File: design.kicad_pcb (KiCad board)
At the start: 2 copper layers, 28.5 x 12 mm, 7 parts, among them J1 USB_C_Receptacle, J2 Conn_01x05, U1 ATtiny1616-M

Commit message: PCB add ID
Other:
- board text added: "<<ID>>"
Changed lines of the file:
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@@
   (general
     (thickness 1.6)
-    (drawings 8)
+    (drawings 9)
     (tracks 0)
     (zones 0)
@@
     )
   )
+  (gr_text <<ID>> (at 151.3 81.8 180) (layer B.SilkS)
+    (effects (font (size 1 1) (thickness 0.15)) (justify mirror))
+  )
   (gr_text <<date>> (at 151.3 86.4 180) (layer B.SilkS)

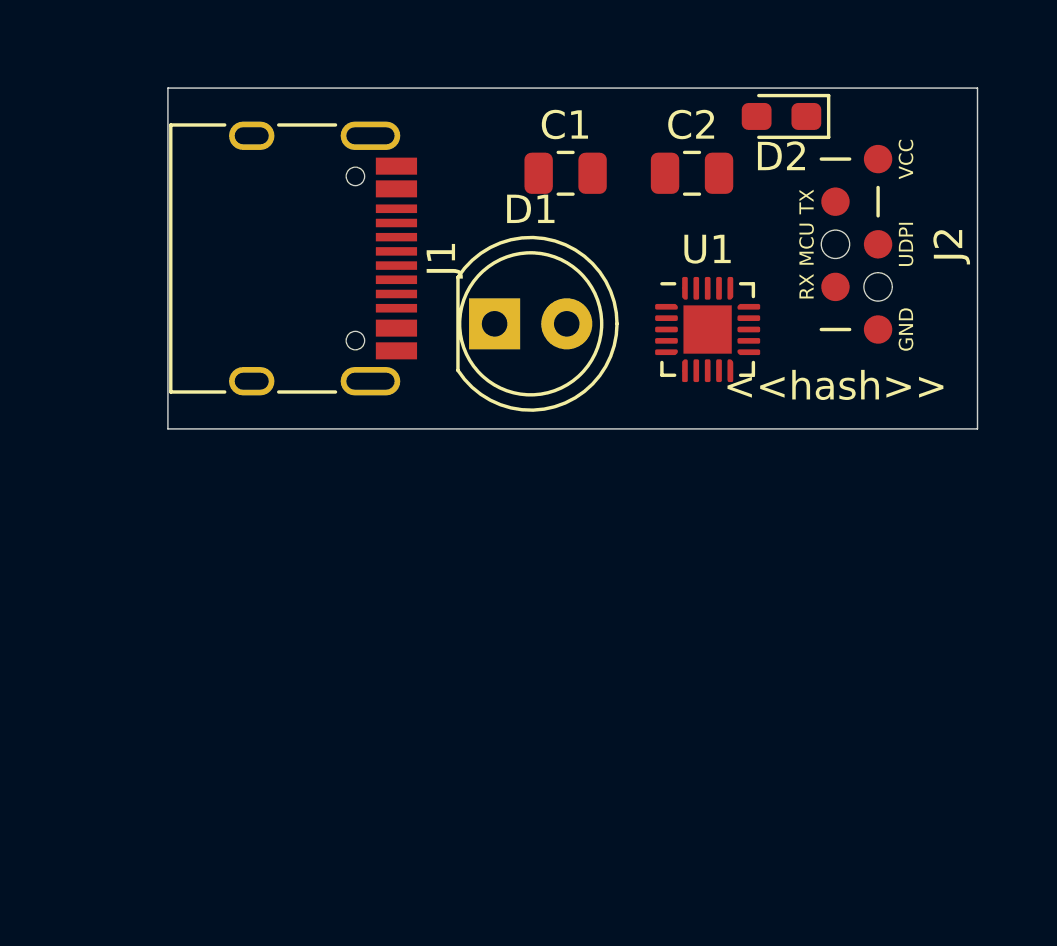
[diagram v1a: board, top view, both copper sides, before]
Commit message: add zone fill
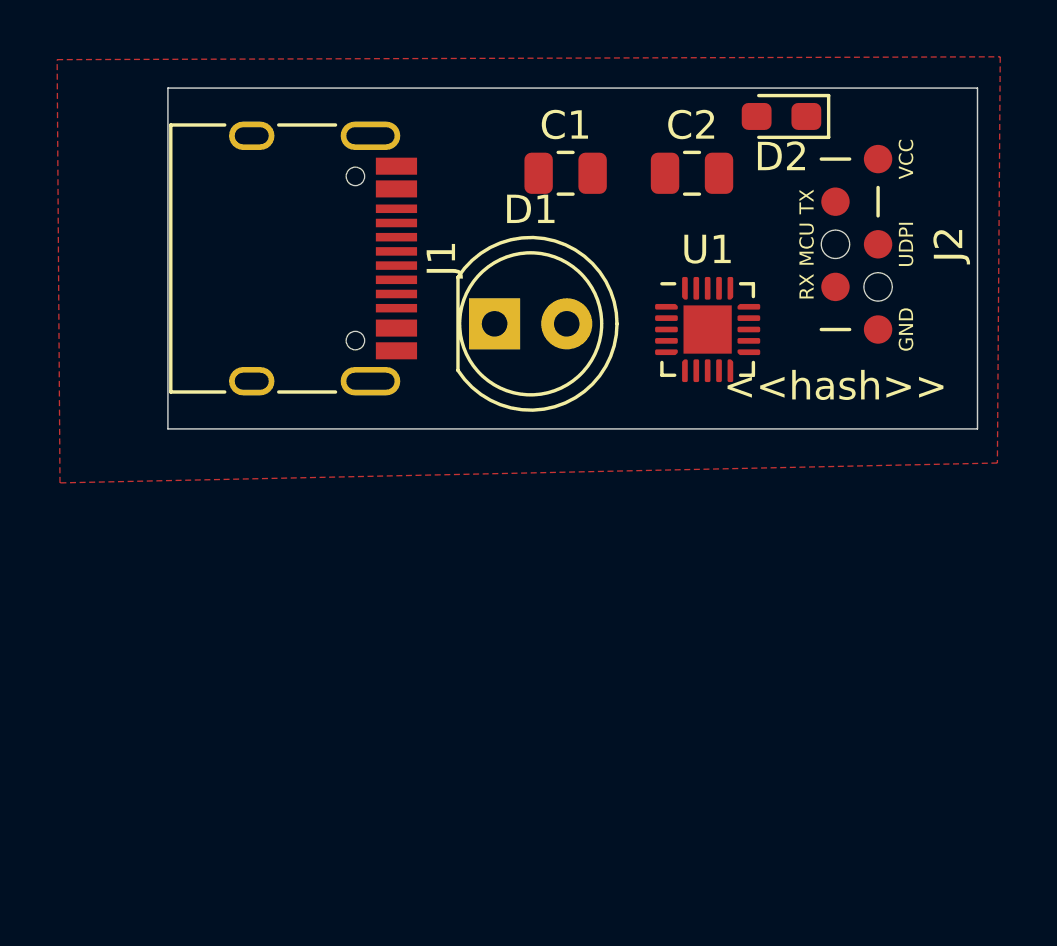
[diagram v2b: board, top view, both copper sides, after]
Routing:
- added copper zone on F.Cu, net Net-(J1-PadA1)

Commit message: Moved to KiCad V6
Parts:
- removed D1: LED, LED_THT:LED_D5.0mm_FlatTop
- removed D2: LED, LED_SMD:LED_0603_1608Metric_Pad1.05x0.95mm_HandSolder
- added C3: C_Small, Capacitor_SMD:C_0805_2012Metric, F.Cu at (144.6, 93.0)
- added C4: C_Small, Capacitor_SMD:C_0805_2012Metric, F.Cu at (144.6, 91.0)
- added J3: Conn_01x03, Connector_PinHeader_2.54mm:PinHeader_1x03_P2.54mm_Vertical, F.Cu at (143.0, 86.6)
- added J4: Conn_01x03, Connector_PinHeader_2.54mm:PinHeader_1x03_P2.54mm_Vertical, F.Cu at (143.0, 84.1)
- added JP1: SolderJumper_2_Open, Jumper:SolderJumper-2_P1.3mm_Open_RoundedPad1.0x1.5mm, F.Cu at (149.0, 99.0)
- added JP2: SolderJumper_2_Open, Jumper:SolderJumper-2_P1.3mm_Open_RoundedPad1.0x1.5mm, F.Cu at (151.5, 99.0)
- added L1: L_Small, Inductor_SMD:L_1008_2520Metric, F.Cu at (144.4, 99.0)
- added R1: R_Small, Resistor_SMD:R_0805_2012Metric, F.Cu at (149.0, 94.5)
- added R2: R_Small, Resistor_SMD:R_0805_2012Metric, F.Cu at (151.5, 94.5)
- J1: value USB_C_Receptacle -> Conn_01x02; footprint Connector_USB:USB_C_Receptacle_HRO_TYPE-C-31-M-12 -> Connector_PinHeader_2.54mm:PinHeader_1x02_P2.54mm_Vertical
- J2: value Conn_01x05 -> Conn_01x02; footprint E32-xxxT20D:UDPI_interface -> Connector_PinHeader_2.54mm:PinHeader_1x02_P2.54mm_Vertical
- U1: value ATtiny1616-M -> TPS61099YFFT; footprint Package_DFN_QFN:VQFN-20-1EP_3x3mm_P0.4mm_EP1.7x1.7mm -> Converter_DCDC_custom:BGA6N40P3X2_122X88X62N
- moved J2 28.3 mm to (143.0, 106.9), turned to 90 degrees
- moved J1 18.6 mm to (143.0, 104.4), turned to 90 degrees
- moved C2 18.0 mm to (142.5, 96.0), turned to 90 degrees
- moved C1 16.3 mm to (140.6, 96.0), turned to 90 degrees
- moved U1 12.5 mm to (145.5, 96.0), turned to 90 degrees
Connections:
- C1 pad 1: Net-(C1-Pad1) -> Vin
- C1 pad 2: Net-(C1-Pad2) -> GND
- C2 pad 1: Net-(C2-Pad1) -> Vin
- C2 pad 2: Net-(C2-Pad2) -> GND
- J2 pad 1: Net-(J2-Pad1) -> Vin
- J2 pad 2: Net-(J2-Pad2) -> GND
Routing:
- net En: track 0.00 -> 19.9 mm, vias 0 -> 1
- net Vin: track 0.00 -> 14.5 mm, vias 0 -> 2
- net FB: track 0.00 -> 8.82 mm
- net GND: track 0.00 -> 3.05 mm, vias 0 -> 31
- net Vout: track 0.00 -> 2.80 mm
- net SW: track 0.00 -> 2.80 mm
- added copper zone on B.Cu, net GND
- added copper zone on F.Cu, net GND
- added copper zone on F.Cu, net SW
- added copper zone on F.Cu, net Vin
- added copper zone on F.Cu, net Vout
- removed copper zone on F.Cu, net Net-(J1-PadA1)
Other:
- board size 28.5 x 12 mm -> 25 x 22.9 mm
- net class Default removed
- board text added: "<<project_name>> <<ID>> <<version>> <<date>> <<hash>> gll.wf/p/001"
- board text added: "EN"
- board text added: "GND"
- board text added: "Vin"
- board text added: "Vout"
- board text removed: "<<ID>>"
- board text removed: "<<date>>"
- board text removed: "<<hash>>"
- board text removed: "<<project_name>>"
- board text removed: "<<version>>"

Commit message: Move website Link in porject.properties
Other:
- board text added: "<<project_name>> <<ID>> <<version>> <<date>> <<hash>> <<website_link>>"
- board text removed: "<<project_name>> <<ID>> <<version>> <<date>> <<hash>> gll.wf/p/001"
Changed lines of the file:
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@@
   )
   (gr_rect (start 134 84.074) (end 159 106.934) (layer "Edge.Cuts") (width 0.05) (fill none))
-  (gr_text "<<project_name>>\n<<ID>>\n<<version>>\n<<date>>\n<<hash>>\ngll.wf/p/001" (at 146.5 95.504) (layer "B.SilkS")
+  (gr_text "<<project_name>>\n<<ID>>\n<<version>>\n<<date>>\n<<hash>>\n<<website_link>>" (at 146.5 95.504) (layer "B.SilkS")
     (effects (font (size 1 1) (thickness 0.15)) (justify mirror))
   )

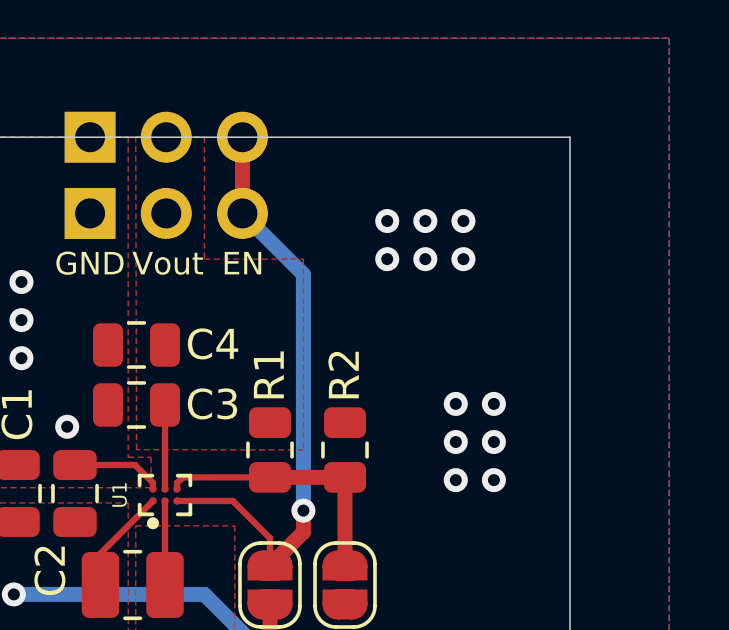
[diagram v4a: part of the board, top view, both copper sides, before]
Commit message: PCB Add Test Via
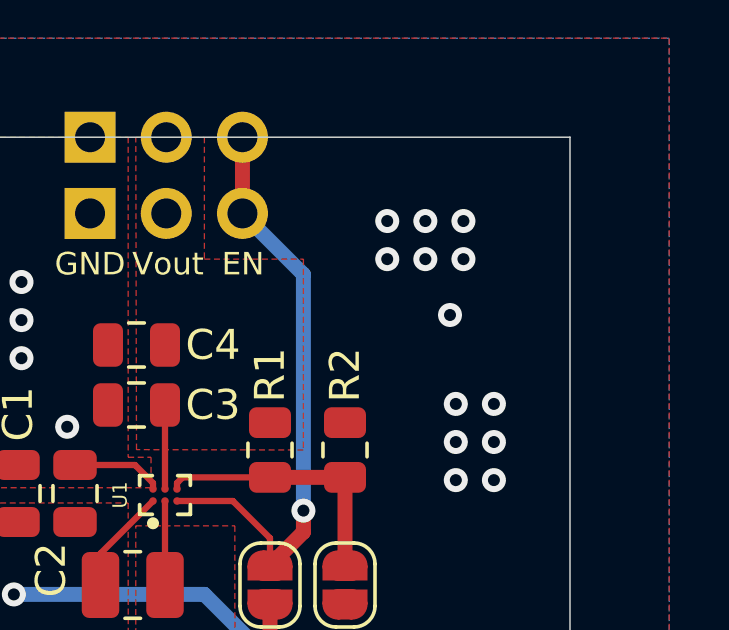
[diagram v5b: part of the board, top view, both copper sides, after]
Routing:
- net GND: vias 31 -> 32
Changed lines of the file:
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@@
   (via (at 155.194 95.504) (size 0.8) (drill 0.4) (layers "F.Cu" "B.Cu") (free) (net 2))
   (via (at 138.176 88.9) (size 0.8) (drill 0.4) (layers "F.Cu" "B.Cu") (free) (net 2))
+  (via (at 155 90) (size 0.8) (drill 0.4) (layers "F.Cu" "B.Cu") (free) (net 2))
   (via (at 155.448 104.648) (size 0.8) (drill 0.4) (layers "F.Cu" "B.Cu") (free) (net 2))
   (via (at 138.176 91.44) (size 0.8) (drill 0.4) (layers "F.Cu" "B.Cu") (free) (net 2))

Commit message: test change for kibot diff
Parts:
- moved J1 4.96 mm to (148.0, 104.4)
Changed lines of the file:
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@@
   )
   (footprint "Connector_PinHeader_2.54mm:PinHeader_1x02_P2.54mm_Vertical" (layer "F.Cu")
-    (at 143.002 104.394 90)
+    (at 147.96 104.394 90)
     (descr "Through hole straight pin header, 1x02, 2.54mm pitch, single row")
     (tags "Through hole pin header THT 1x02 2.54mm single row")
